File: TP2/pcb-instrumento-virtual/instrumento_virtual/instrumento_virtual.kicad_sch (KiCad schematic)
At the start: 55 parts, among them J1 socket_entradas_digitales, J2 Conn_salidas_analogicas, J3 Conn_01x20_Socket, J4 Conn_01x02_Socket, J5 Conn_01x20_Socket, J6 salidas_digitales, J7 RS232, U1 CD4051B, U2 MCP6001R, U3 MCP6001R, U4 AMS1117-5.0

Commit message: primera versión tentativa de esquemático
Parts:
- removed C6: 100nF, symbol Device:C
- removed J1: socket_entradas_digitales, symbol Connector:Conn_01x08_Socket
- removed J2: Conn_salidas_analogicas, symbol Connector:Conn_01x02_Socket
- removed J4: Conn_01x02_Socket, symbol Connector:Conn_01x02_Socket
- removed J6: salidas_digitales, symbol Connector:Conn_01x08_Socket
- removed U2, U3: MCP6001R, Package_TO_SOT_SMD:SOT-23-5, symbol Amplifier_Operational:MCP6001R
- removed U4: AMS1117-5.0, Package_TO_SOT_SMD:SOT-223-3_TabPin2, symbol Regulator_Linear:AMS1117-5.0
- added C15: 100u, Capacitor_THT:CP_Radial_D6.3mm_P2.50mm, symbol Device:C
- added C16, C17: 100n, Capacitor_THT:C_Disc_D6.0mm_W2.5mm_P5.00mm, symbol Device:C
- added C18: 10u, Capacitor_THT:CP_Radial_D5.0mm_P2.50mm, symbol Device:C
- added J1, J4: Conn_01x09_Pin, Connector_PinHeader_2.54mm:PinHeader_1x09_P2.54mm_Vertical, symbol Connector:Conn_01x09_Pin
- added J2: Conector_salidas_analógicas, Connector_PinHeader_2.54mm:PinHeader_1x03_P2.54mm_Vertical, symbol Connector:Conn_01x03_Pin
- added Q10, Q3, Q4, Q5, Q6, Q7, Q8, Q9: BC547, Package_TO_SOT_THT:TO-92_Inline, symbol Transistor_BJT:BC547
- added R27, R30: 100k, Resistor_THT:R_Box_L8.4mm_W2.5mm_P5.08mm, symbol Device:R
- added R28: 1k, Resistor_THT:R_Box_L8.4mm_W2.5mm_P5.08mm, symbol Device:R
- added R29: 150k, Resistor_THT:R_Box_L8.4mm_W2.5mm_P5.08mm, symbol Device:R
- added R31, R32, R33, R35, R36, R37, R43, R45: 2.2k, Resistor_THT:R_Box_L8.4mm_W2.5mm_P5.08mm, symbol Device:R
- added R34, R38, R39, R40, R41, R42, R44, R46: 6.8k, Resistor_THT:R_Box_L8.4mm_W2.5mm_P5.08mm, symbol Device:R
- added R47: 68K, Resistor_THT:R_Box_L8.4mm_W2.5mm_P5.08mm, symbol Device:R
- added R48: 33K, Resistor_THT:R_Box_L8.4mm_W2.5mm_P5.08mm, symbol Device:R
- added R49: 10K, Resistor_THT:R_Box_L8.4mm_W2.5mm_P5.08mm, symbol Device:R
- added RV1: 10K, Resistor_THT:R_Box_L8.4mm_W2.5mm_P5.08mm, symbol Device:R_Potentiometer
- added U2, U6: MCP6002-xMC, Package_DIP:DIP-8_W7.62mm, symbol Amplifier_Operational:MCP6002-xMC
- added U4: AMS1117-3.3, Package_TO_SOT_SMD:SOT-223-3_TabPin2, symbol Regulator_Linear:AMS1117-3.3
- added U5: AMS1117-5.0, Package_TO_SOT_SMD:SOT-223-3_TabPin2, symbol Regulator_Linear:AMS1117-5.0
- C1: value 10u -> 100n; footprint (none) -> Capacitor_THT:C_Disc_D6.0mm_W2.5mm_P5.00mm
- C10, C11, C12, C13, C14, C7, C8, C9: footprint (none) -> Capacitor_THT:C_Disc_D6.0mm_W2.5mm_P5.00mm
- C2: value 100n -> 10u; footprint (none) -> Capacitor_THT:CP_Radial_D5.0mm_P2.50mm
- C3: footprint (none) -> Capacitor_THT:CP_Radial_D5.0mm_P2.50mm
- C4: value 10u -> 22u; footprint (none) -> Capacitor_THT:CP_Radial_D5.0mm_P2.50mm
- C5: value 100nF -> 22u; footprint (none) -> Capacitor_THT:CP_Radial_D5.0mm_P2.50mm
- J3, J5: footprint (none) -> Connector_PinHeader_2.54mm:PinHeader_1x20_P2.54mm_Vertical
- J7: footprint (none) -> Connector_PinHeader_2.54mm:PinHeader_1x09_P2.54mm_Vertical
- R1: value 68K -> 1M; footprint (none) -> Resistor_THT:R_Box_L8.4mm_W2.5mm_P5.08mm
- R10: value 1K -> 150k; footprint (none) -> Resistor_THT:R_Box_L8.4mm_W2.5mm_P5.08mm
- R11, R12, R13, R14, R15, R16, R17, R18, R19, R20, R21, R22, R23, R24, R25, R26: footprint (none) -> Resistor_THT:R_Box_L8.4mm_W2.5mm_P5.08mm
- R2: value 33K -> 1M; footprint (none) -> Resistor_THT:R_Box_L8.4mm_W2.5mm_P5.08mm
- R3, R4: value 100k -> 1M; footprint (none) -> Resistor_THT:R_Box_L8.4mm_W2.5mm_P5.08mm
- R5: value 33k -> 68k; footprint (none) -> Resistor_THT:R_Box_L8.4mm_W2.5mm_P5.08mm
- R6, R7: value 10K -> 680; footprint (none) -> Resistor_THT:R_Box_L8.4mm_W2.5mm_P5.08mm
- R8: value 33K -> 33k; footprint (none) -> Resistor_THT:R_Box_L8.4mm_W2.5mm_P5.08mm
- R9: value 1K -> 1k; footprint (none) -> Resistor_THT:R_Box_L8.4mm_W2.5mm_P5.08mm
- U1: footprint (none) -> Package_DIP:DIP-16_W7.62mm_LongPads
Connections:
- net VDD is gone; now on net +12V: U1.16 (VDD)
- net +12V: now also C3.1, C15.1, C16.1, U4.3 (VI), U5.3 (VI); no longer C1.1, C2.1
- net AOUT01: now also R10.1, J2.1 (Pin_1), U6.1; no longer C5.1, R9.2
- net AOUT02: now also J2.2 (Pin_2), R29.1, U6.7; no longer R10.2
- net GND: now also R4.2, R8.2, C15.2, C16.2, C17.2, C18.2, J1.9 (Pin_9), J2.3 (Pin_3), J4.1 (Pin_1), R27.2, R30.2, R48.2, RV1.2, RV1.3, U2.4 (V-), U2.9 (V-), U4.1 (GND), U5.1 (GND), U6.4 (V-), U6.9 (V-); no longer R2.2, R5.2
- net IN01: now also J1.1 (Pin_1)
- net IN02: now also J1.2 (Pin_2)
- net IN03: now also J1.3 (Pin_3)
- net IN04: now also J1.4 (Pin_4)
- net IN05: now also J1.5 (Pin_5)
- net IN06: now also J1.6 (Pin_6)
- net IN07: now also J1.7 (Pin_7)
- net PA1: now also U2.6 (-), U2.7; no longer D3.2 (A), D4.1 (K), R7.2
- net PA10: now also Q9.3 (E)
- net PA15: now also Q4.3 (E)
- net PA2: now also C13.1, R22.2, R26.2
- net PA3: now also C12.1, R21.2, R25.2
- net PA4: now also C11.1, R20.2, R24.2
- net PA5: now also C10.1, R19.2, R23.2
- net PA6: now also C9.1, R16.2, R18.2
- net PA7: now also C8.1, R15.2, R17.2
- net PA8: now also Q5.3 (E); no longer U1.9 (C)
- net PA9: now also Q7.3 (E)
- net PB0: now also C7.1, R13.2, R14.2
- net PB1: now also C14.1, R11.2, R12.2
- net PB12: now also U1.11 (A)
- net PB13: now also U1.10 (B)
- net PB14: now also U1.9 (C); no longer U1.11 (A)
- net PB15: now also Q3.3 (E); no longer U1.10 (B)
- net PB3: now also Q6.3 (E)
- net PB4: now also Q8.3 (E); no longer R9.1
- net PB5: now also Q10.3 (E); no longer R10.1
- net PB6: now also R9.1
- net PB7: now also R28.1
- net at R2.1: now also R1.1, U2.2 (-); no longer R1.2
- net +/-5V: now reaches R5.1
- net +/-5V: now also R22.1, J1.8 (Pin_8); no longer R4.2
- net at R3.2: now also R4.1, U2.3 (+); no longer R8.2
- removed net 5V: C3.1, C4.1, J5.18 (Pin_18), R4.1
- net AIN01 renamed MUX_OUT
- net MUX_OUT: now also R47.1; no longer R1.1
- net CH01: no longer names the net of R6.1
- net CH01: now also R1.2, U2.1
- net CH02: no longer names the net of R8.1
- net CH02: now also R2.2, R5.2; no longer R7.1
- net IN08 renamed OFFSET
- net OFFSET: now also R49.2, RV1.1; no longer R22.1
- new net: C4.1, R9.2, U6.3 (+)
- new net: Q8.2 (B), R43.2
- new net: Q3.2 (B), R31.2
- new net: R29.2, R30.1, U6.6 (-)
- new net: Q6.2 (B), R36.2
- new net: Q9.2 (B), R37.2
- new net: D3.2 (A), D4.1 (K), R7.2, U2.5 (+)
- new net: R47.2, R48.1, R7.1
- new net: Q7.2 (B), R35.2
- new net: Q10.2 (B), R45.2
- new net: Q5.2 (B), R33.2
- new net: C5.1, R28.2, U6.5 (+)
- new net: R10.2, R27.1, U6.2 (-)
- new net: Q4.2 (B), R32.2
- new net +3.3V: C17.1, C18.1, R49.1, U2.8 (V+), U4.2 (VO)
- new net +5V: C1.1, C2.1, J5.18 (Pin_18), R34.1, R38.1, R39.1, R40.1, R41.1, R42.1, R44.1, R46.1, U5.2 (VO), U6.8 (V+)
- new net 3.3V: R31.1, R32.1, R33.1, R35.1, R36.1, R37.1, R43.1, R45.1
- new net DOUT1: J4.9 (Pin_9), Q3.1 (C), R39.2
- new net DOUT2: J4.8 (Pin_8), Q5.1 (C), R40.2
- new net DOUT3: J4.7 (Pin_7), Q7.1 (C), R41.2
- new net DOUT4: J4.6 (Pin_6), Q9.1 (C), R42.2
- new net DOUT5: J4.5 (Pin_5), Q4.1 (C), R34.2
- new net DOUT6: J4.4 (Pin_4), Q6.1 (C), R38.2
- new net DOUT7: J4.3 (Pin_3), Q8.1 (C), R44.2
- new net DOUT8: J4.2 (Pin_2), Q10.1 (C), R46.2
- no-connect marks 2 -> 11
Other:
- note added: "Blue Pill"
- note added: "Conversor de niveles lógicos 3.3-5v"
- note added: "entradas analógicas (2)"
- note added: "entradas digitales (8)"
- note added: "salidas analógicas (2)"
- note added: "salidas digitales (8)"
- note added: "salidas para mux"
- moved on the sheet: D1, D2, D3, D4, J3, J5, R6, R7, U1

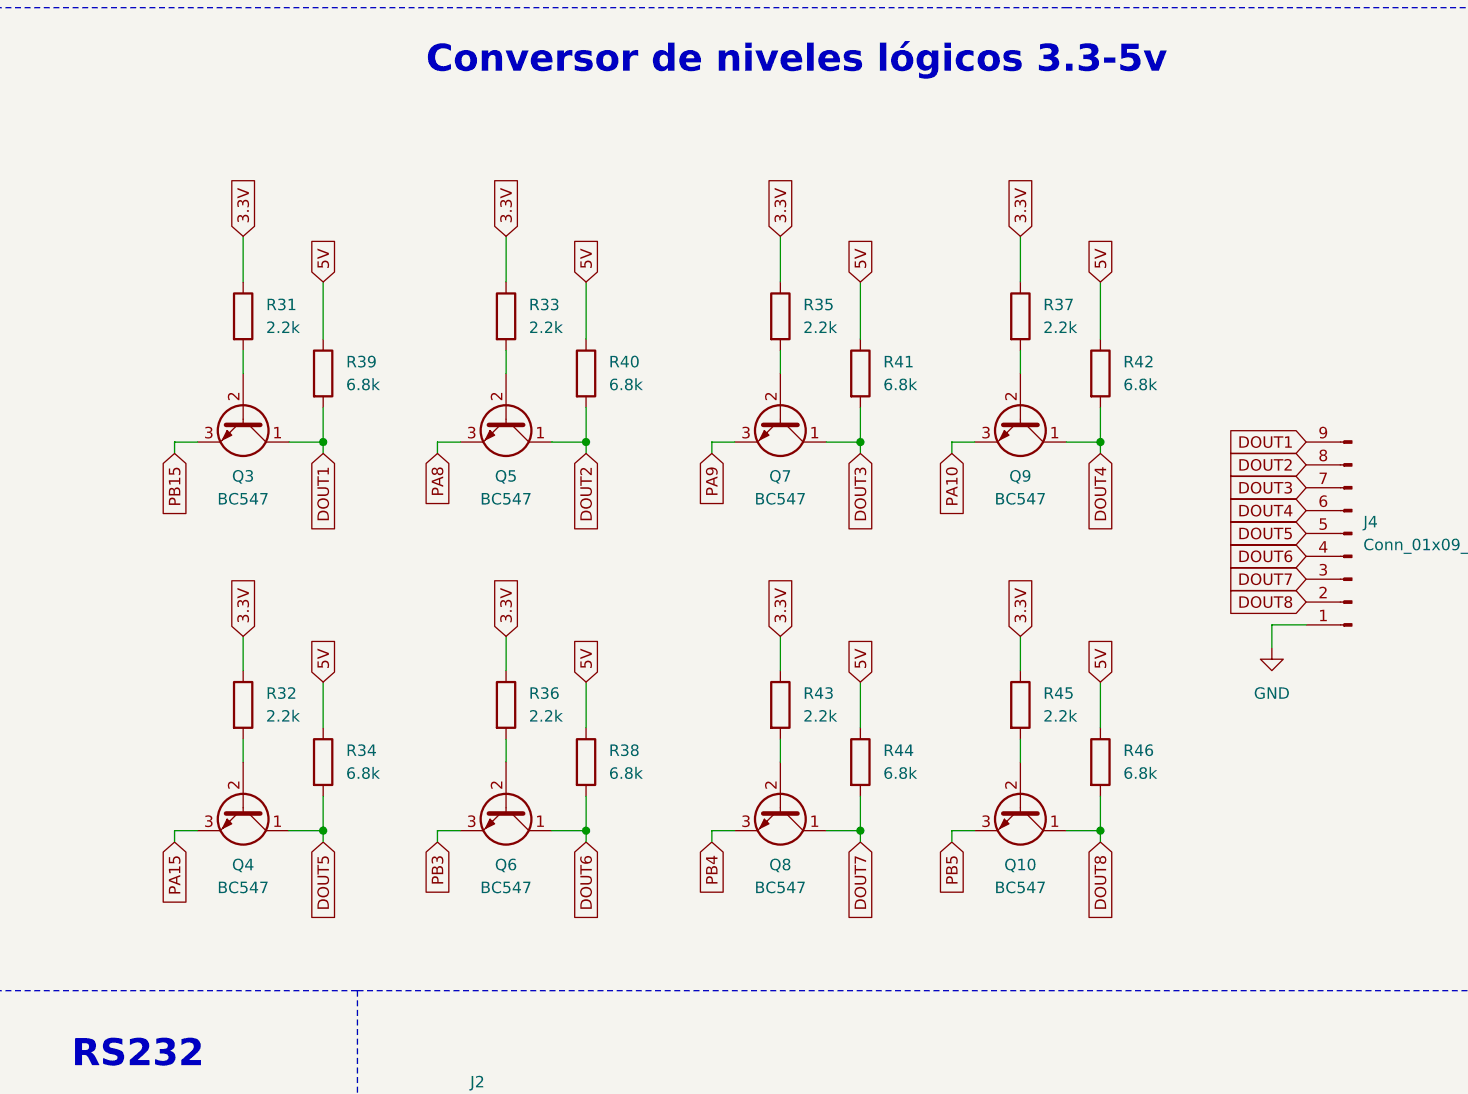
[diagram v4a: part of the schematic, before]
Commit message: cambiado circuito de adaptacion de niveles logicos
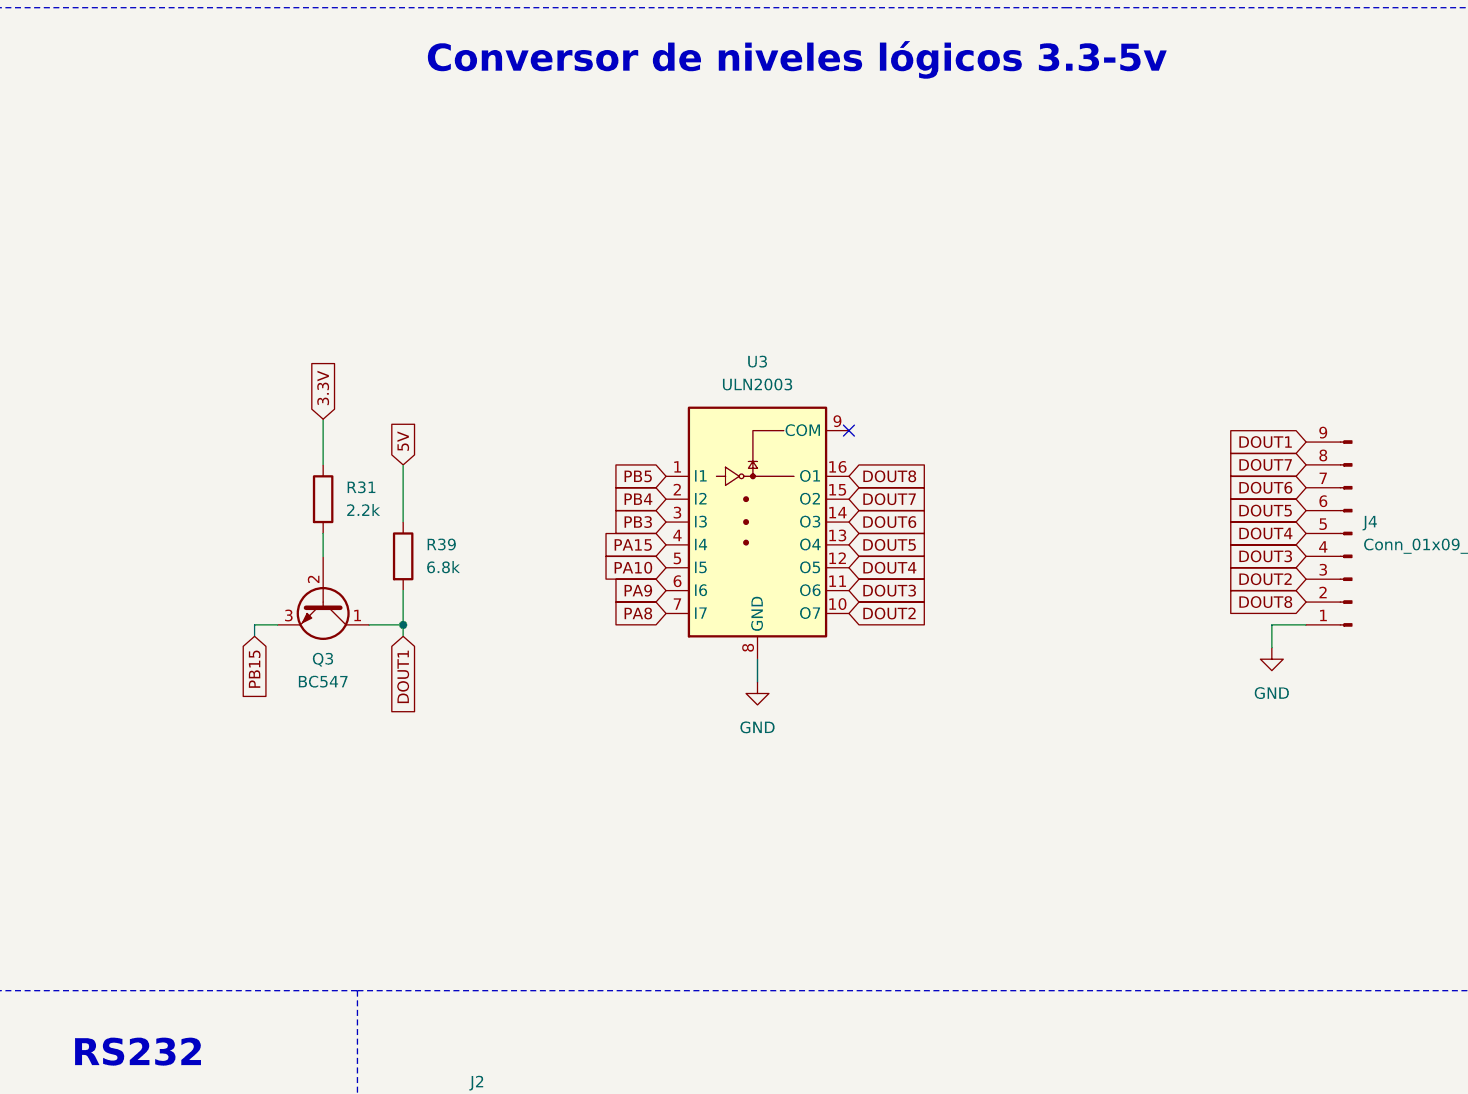
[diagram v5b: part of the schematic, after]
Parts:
- removed Q10, Q4, Q5, Q6, Q7, Q8, Q9: BC547, Package_TO_SOT_THT:TO-92_Inline, symbol Transistor_BJT:BC547
- removed R32, R33, R35, R36, R37, R43, R45: 2.2k, Resistor_THT:R_Box_L8.4mm_W2.5mm_P5.08mm, symbol Device:R
- removed R34, R38, R40, R41, R42, R44, R46: 6.8k, Resistor_THT:R_Box_L8.4mm_W2.5mm_P5.08mm, symbol Device:R
- added U3: ULN2003, Package_DIP:DIP-16_W7.62mm_LongPads, symbol Transistor_Array:ULN2003
- J7: footprint Connector_PinHeader_2.54mm:PinHeader_1x09_P2.54mm_Vertical -> Connector_PinHeader_2.54mm:PinHeader_1x03_P2.54mm_Vertical
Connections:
- net DOUT2: now also J4.3 (Pin_3), U3.10 (O7); no longer J4.8 (Pin_8)
- net DOUT3: now also J4.4 (Pin_4), U3.11 (O6); no longer J4.7 (Pin_7)
- net DOUT4: now also J4.5 (Pin_5), U3.12 (O5); no longer J4.6 (Pin_6)
- net DOUT5: now also J4.6 (Pin_6), U3.13 (O4); no longer J4.5 (Pin_5)
- net DOUT6: now also J4.7 (Pin_7), U3.14 (O3); no longer J4.4 (Pin_4)
- net DOUT7: now also J4.8 (Pin_8), U3.15 (O2); no longer J4.3 (Pin_3)
- net DOUT8: now also U3.16 (O1)
- net GND: now also U3.8 (GND)
- net PA10: now also U3.5 (I5)
- net PA15: now also U3.4 (I4)
- net PA8: now also U3.7 (I7)
- net PA9: now also U3.6 (I6)
- net PB3: now also U3.3 (I3)
- net PB4: now also U3.2 (I2)
- net PB5: now also U3.1 (I1)
- no-connect marks 11 -> 12
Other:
- moved on the sheet: Q3, R31, R39
